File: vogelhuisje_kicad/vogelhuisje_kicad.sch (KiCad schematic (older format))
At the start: 0 parts

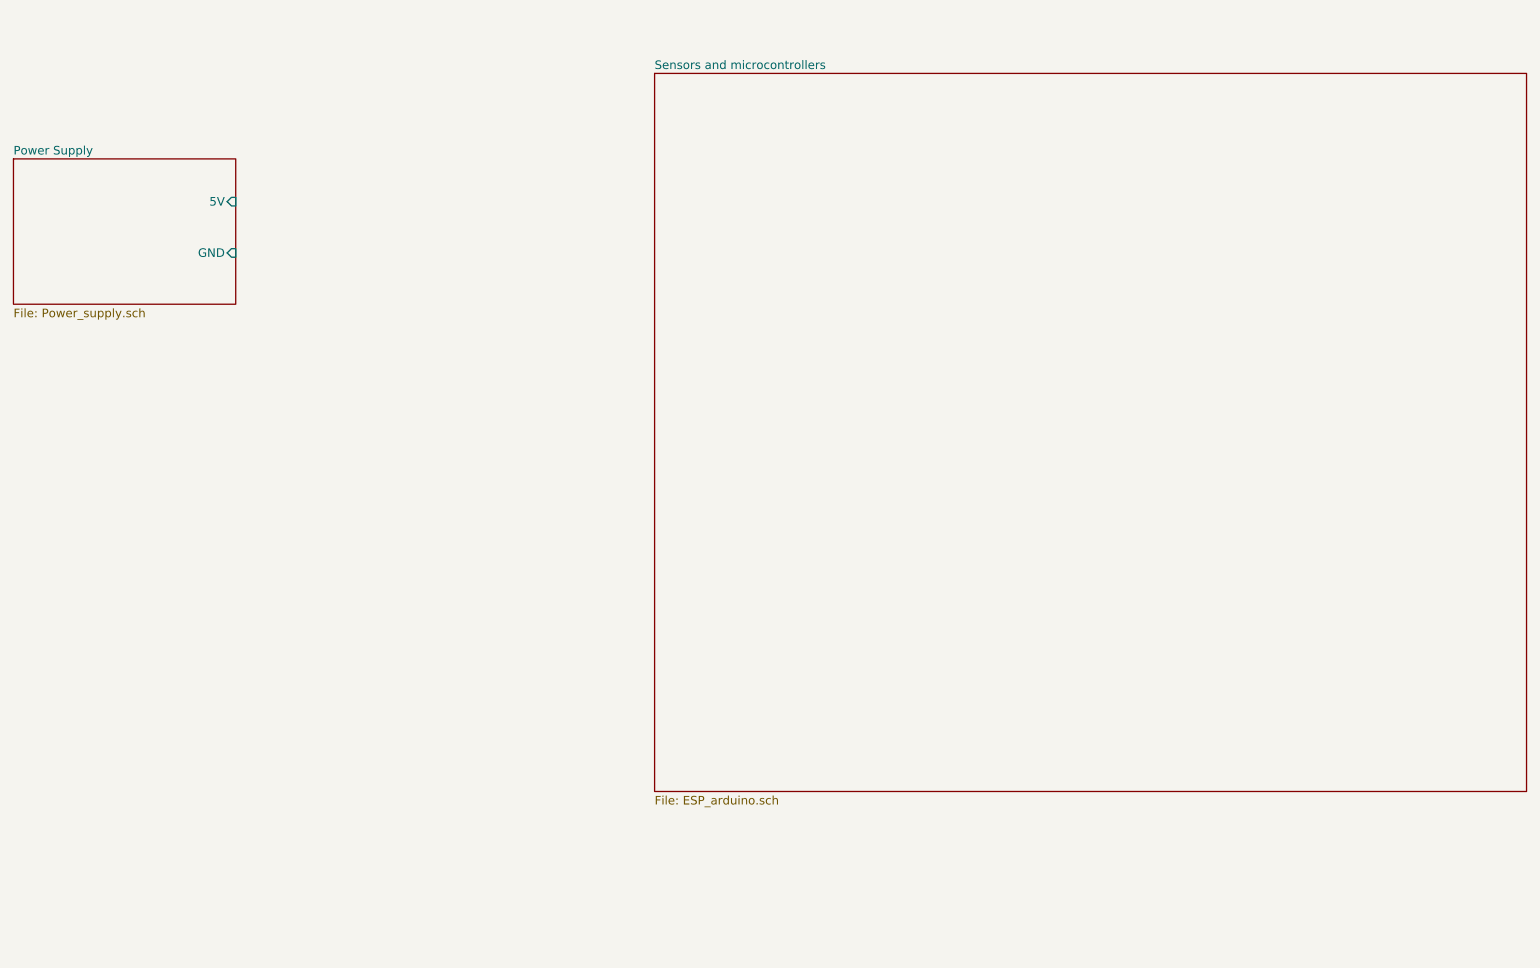
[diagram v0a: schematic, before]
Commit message: Add Camera to schematic
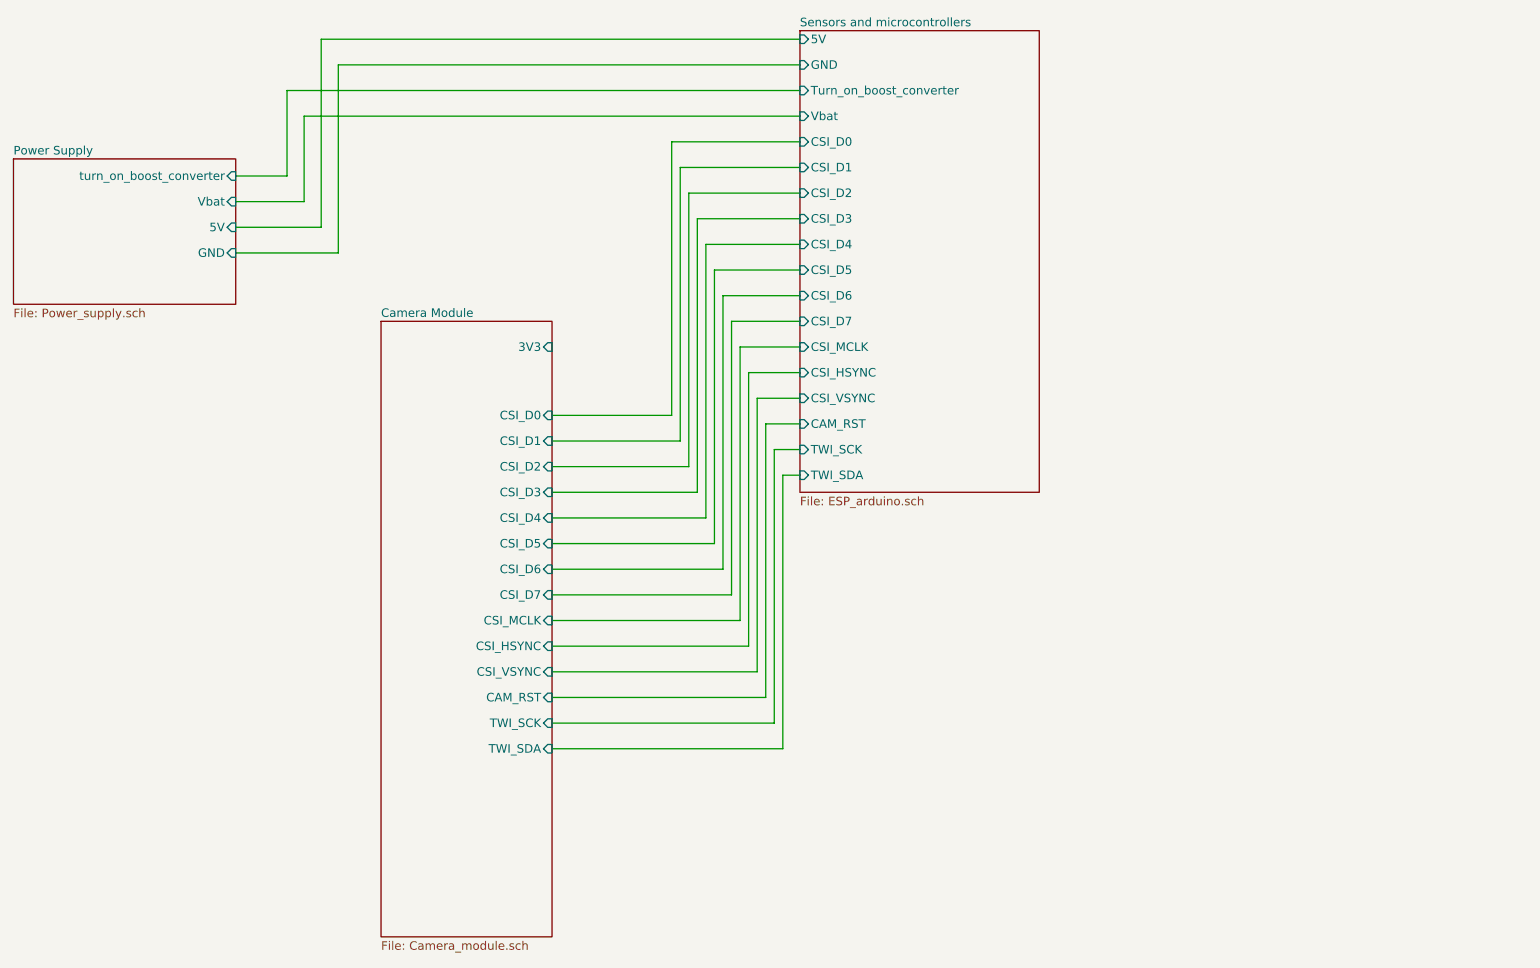
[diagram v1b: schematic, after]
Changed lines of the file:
@@
 $Descr A4 11693 8268
 encoding utf-8
-Sheet 1 3
+Sheet 1 4
 Title ""
 Date ""
@@
 F0 "Power Supply" 50
 F1 "Power_supply.sch" 50
-F2 "5V" I R 3000 2550 50
+F2 "5V" I R 3000 2700 50
 F3 "GND" I R 3000 2850 50
+F4 "turn_on_boost_converter" I R 3000 2400 50
+F5 "Vbat" I R 3000 2550 50
 $EndSheet
 $Sheet
-S 5450 1800 5100 4200
+S 6300 1550 1400 2700
 U 6263B902
 F0 "Sensors and microcontrollers" 50
 F1 "ESP_arduino.sch" 50
+F2 "GND" I L 6300 1750 50
+F3 "5V" I L 6300 1600 50
+F4 "CSI_D0" I L 6300 2200 50
+F5 "CSI_D1" I L 6300 2350 50
+F6 "CSI_D2" I L 6300 2500 50
+F7 "CSI_D3" I L 6300 2650 50
+F8 "CSI_D4" I L 6300 2800 50
+F9 "CSI_D5" I L 6300 2950 50
+F10 "CSI_D6" I L 6300 3100 50
+F11 "CSI_D7" I L 6300 3250 50
+F12 "CSI_MCLK" I L 6300 3400 50
+F13 "CSI_HSYNC" I L 6300 3550 50
+F14 "CSI_VSYNC" I L 6300 3700 50
+F15 "CAM_RST" I L 6300 3850 50
+F16 "TWI_SCK" I L 6300 4000 50
+F17 "TWI_SDA" I L 6300 4150 50
+F18 "Vbat" I L 6300 2050 50
+F19 "Turn_on_boost_converter" I L 6300 1900 50
 $EndSheet
+Wire Wire Line
+	6300 1900 3300 1900
+Wire Wire Line
+	3300 1900 3300 2400
+Wire Wire Line
+	3300 2400 3000 2400
+Wire Wire Line
+	3000 2550 3400 2550
+Wire Wire Line
+	3400 2550 3400 2050
+Wire Wire Line
+	3400 2050 6300 2050
+Wire Wire Line
+	3000 2700 3500 2700
+Wire Wire Line
+	3500 2700 3500 1600
+Wire Wire Line
+	3500 1600 6300 1600
+Wire Wire Line
+	3000 2850 3600 2850
+Wire Wire Line
+	3600 2850 3600 1750
+Wire Wire Line
+	3600 1750 6300 1750
+$Sheet
+S 3850 3250 1000 3600
+U 626EFA13
+F0 "Camera Module" 50
+F1 "Camera_module.sch" 50
+F2 "CSI_D0" I R 4850 3800 50
+F3 "CSI_D1" I R 4850 3950 50
+F4 "CSI_D2" I R 4850 4100 50
+F5 "CSI_D3" I R 4850 4250 50
+F6 "CSI_D4" I R 4850 4400 50
+F7 "CSI_D5" I R 4850 4550 50
+F8 "CSI_D6" I R 4850 4700 50
+F9 "CSI_D7" I R 4850 4850 50
+F10 "CSI_MCLK" I R 4850 5000 50
+F11 "CSI_HSYNC" I R 4850 5150 50
+F12 "CSI_VSYNC" I R 4850 5300 50
+F13 "CAM_RST" I R 4850 5450 50
+F14 "TWI_SCK" I R 4850 5600 50
+F15 "TWI_SDA" I R 4850 5750 50
+F16 "3V3" I R 4850 3400 50
+$EndSheet
+Wire Wire Line
+	6300 4150 6200 4150
+Wire Wire Line
+	6200 4150 6200 5750
+Wire Wire Line
+	6200 5750 4850 5750
+Wire Wire Line
+	4850 5600 6150 5600
+Wire Wire Line
+	6150 5600 6150 4000
+Wire Wire Line
+	6150 4000 6300 4000
+Wire Wire Line
+	6300 3850 6100 3850
+Wire Wire Line
+	6100 3850 6100 5450
+Wire Wire Line
+	6100 5450 4850 5450
+Wire Wire Line
+	4850 5300 6050 5300
+Wire Wire Line
+	6050 5300 6050 3700
+Wire Wire Line
+	6050 3700 6300 3700
+Wire Wire Line
+	6300 3550 6000 3550
+Wire Wire Line
+	6000 3550 6000 5150
+Wire Wire Line
+	6000 5150 4850 5150
+Wire Wire Line
+	4850 5000 5950 5000
+Wire Wire Line
+	5950 5000 5950 3400
+Wire Wire Line
+	5950 3400 6300 3400
+Wire Wire Line
+	6300 3250 5900 3250
+Wire Wire Line
+	5900 3250 5900 4850
+Wire Wire Line
+	5900 4850 4850 4850
+Wire Wire Line
+	4850 4700 5850 4700
+Wire Wire Line
+	5850 4700 5850 3100
+Wire Wire Line
+	5850 3100 6300 3100
+Wire Wire Line
+	4850 4550 5800 4550
+Wire Wire Line
+	5800 4550 5800 2950
+Wire Wire Line
+	5800 2950 6300 2950
+Wire Wire Line
+	4850 4400 5750 4400
+Wire Wire Line
+	5750 4400 5750 2800
+Wire Wire Line
+	5750 2800 6300 2800
+Wire Wire Line
+	4850 4250 5700 4250
+Wire Wire Line
+	5700 4250 5700 2650
+Wire Wire Line
+	5700 2650 6300 2650
+Wire Wire Line
+	4850 4100 5650 4100
+Wire Wire Line
+	5650 4100 5650 2500
+Wire Wire Line
+	5650 2500 6300 2500
+Wire Wire Line
+	4850 3950 5600 3950
+Wire Wire Line
+	5600 3950 5600 2350
+Wire Wire Line
+	5600 2350 6300 2350
+Wire Wire Line
+	4850 3800 5550 3800
+Wire Wire Line
+	5550 3800 5550 2200
+Wire Wire Line
+	5550 2200 6300 2200
 $EndSCHEMATC

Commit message: Update Camera_module.sch, Camera_module.sch-bak, and 5 more files...
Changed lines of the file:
@@
 $EndSheet
 $Sheet
-S 6300 1550 1400 2700
+S 6300 1550 1650 3300
 U 6263B902
 F0 "Sensors and microcontrollers" 50
@@
 F18 "Vbat" I L 6300 2050 50
 F19 "Turn_on_boost_converter" I L 6300 1900 50
+F20 "V_LED_switch-" I L 6300 4300 50
+F21 "3V3" I L 6300 4450 50
 $EndSheet
 Wire Wire Line
@@
 	3400 2550 3400 2050
 Wire Wire Line
-	3400 2050 6300 2050
+	3400 2050 5150 2050
 Wire Wire Line
 	3000 2700 3500 2700
@@
 Wire Wire Line
 	3600 1750 6300 1750
-$Sheet
-S 3850 3250 1000 3600
-U 626EFA13
-F0 "Camera Module" 50
-F1 "Camera_module.sch" 50
-F2 "CSI_D0" I R 4850 3800 50
-F3 "CSI_D1" I R 4850 3950 50
-F4 "CSI_D2" I R 4850 4100 50
-F5 "CSI_D3" I R 4850 4250 50
-F6 "CSI_D4" I R 4850 4400 50
-F7 "CSI_D5" I R 4850 4550 50
-F8 "CSI_D6" I R 4850 4700 50
-F9 "CSI_D7" I R 4850 4850 50
-F10 "CSI_MCLK" I R 4850 5000 50
-F11 "CSI_HSYNC" I R 4850 5150 50
-F12 "CSI_VSYNC" I R 4850 5300 50
-F13 "CAM_RST" I R 4850 5450 50
-F14 "TWI_SCK" I R 4850 5600 50
-F15 "TWI_SDA" I R 4850 5750 50
-F16 "3V3" I R 4850 3400 50
-$EndSheet
 Wire Wire Line
 	6300 4150 6200 4150
@@
 Wire Wire Line
 	5550 2200 6300 2200
+Wire Wire Line
+	6300 4450 5300 4450
+Wire Wire Line
+	5300 3350 4850 3350
+$Sheet
+S 3850 3250 1000 3600
+U 626EFA13
+F0 "Camera Module" 50
+F1 "Camera_module.sch" 50
+F2 "CSI_D0" I R 4850 3800 50
+F3 "CSI_D1" I R 4850 3950 50
+F4 "CSI_D2" I R 4850 4100 50
+F5 "CSI_D3" I R 4850 4250 50
+F6 "CSI_D4" I R 4850 4400 50
+F7 "CSI_D5" I R 4850 4550 50
+F8 "CSI_D6" I R 4850 4700 50
+F9 "CSI_D7" I R 4850 4850 50
+F10 "CSI_MCLK" I R 4850 5000 50
+F11 "CSI_HSYNC" I R 4850 5150 50
+F12 "CSI_VSYNC" I R 4850 5300 50
+F13 "CAM_RST" I R 4850 5450 50
+F14 "TWI_SCK" I R 4850 5600 50
+F15 "TWI_SDA" I R 4850 5750 50
+F16 "3V3" I R 4850 3350 50
+F17 "V_led_switch-" I R 4850 3650 50
+F18 "Vbat" I R 4850 3500 50
+$EndSheet
+Wire Wire Line
+	5300 3350 5300 4450
+Wire Wire Line
+	4850 3500 5150 3500
+Wire Wire Line
+	5150 3500 5150 2050
+Connection ~ 5150 2050
+Wire Wire Line
+	5150 2050 6300 2050
+Wire Wire Line
+	4850 3650 5450 3650
+Wire Wire Line
+	5450 3650 5450 4300
+Wire Wire Line
+	5450 4300 6300 4300
 $EndSCHEMATC
